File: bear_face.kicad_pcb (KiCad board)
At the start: 2 copper layers, 301.7 x 112.6 mm, 192 parts, among them J1 USB_B_Micro, SW1 SW_Push, U1 ATmega32U4-AU, Y1 16MHz

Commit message: Initial SMD commit
Diodes changed to SMD, short tracks added to pad2 and between adjacent diodes
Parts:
- removed G***: COLE, bear_face_silks:cbf_small_flipped
- removed G***: PASTA, bear_face_silks:pasta_small
- D1, D10, D11, D12, D13, D14, D15, D16, D17, D18, D19, D2, D20, D21, D22, D23, D24, D25, D26, D27, D28, D29, D3, D30, D31, D32, D33, D34, D35, D36, D37, D38, D39, D4, D40, D41, D42, D43, D44, D45, D46, D47, D48, D49, D5, D50, D51, D52, D53, D54, D55, D56, D57, D58, D59, D6, D60, D61, D62, D63, D64, D65, D66, D67, D68, D69, D7, D70, D71, D72, D73, D74, D75, D76, D77, D78, D79, D8, D80, D81, D82, D83, D9: footprint Keebio-Parts:Diode -> bear_face_parts:D_SOD-123; moved to B.Cu
- MX1, MX15, MX31, MX44: footprint MX_Only:MXOnly-1.5U-NoLED -> bear_face_parts:MXOnly-1.5U-NoLED
- MX10, MX11, MX12, MX13, MX14, MX16, MX17, MX18, MX19, MX2, MX20, MX21, MX22, MX23, MX24, MX25, MX26, MX27, MX28, MX3, MX30, MX32, MX33, MX34, MX35, MX36, MX37, MX38, MX39, MX4, MX40, MX41, MX42, MX43, MX45, MX47, MX48, MX49, MX5, MX50, MX51, MX52, MX53, MX54, MX55, MX56, MX57, MX59, MX6, MX61, MX62, MX63, MX64, MX65, MX66, MX67, MX68, MX69, MX7, MX70, MX72, MX73, MX78, MX79, MX8, MX80, MX81, MX82, MX83, MX9: footprint MX_Only:MXOnly-1U-NoLED -> bear_face_parts:MXOnly-1U-NoLED
- MX29: footprint MX_Only:MXOnly-2U-NoLED -> bear_face_parts:MXOnly-2U-NoLED
- MX46, MX71: footprint MX_Only:MXOnly-1.75U-NoLED -> bear_face_parts:MXOnly-1.75U-NoLED
- MX58, MX60: footprint MX_Only:MXOnly-2.25U-NoLED -> bear_face_parts:MXOnly-2.25U-NoLED
- MX74, MX75, MX76: footprint MX_Only:MXOnly-1.25U-NoLED -> bear_face_parts:MXOnly-1.25U-NoLED
- MX77: footprint MX_Only:MXOnly-6.25U-ReversedStabilizers-NoLED -> bear_face_parts:MXOnly-6.25U-ReversedStabilizers-NoLED
- SW1: footprint random-keyboard-parts:PushButton_6x6mm_TH_Pretty -> bear_face_parts:PushButton_6x6mm_TH_Pretty
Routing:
- net ROW0: track 372.4 -> 17.8 mm
- net ROW1: track 355.8 -> 15.2 mm, vias 2 -> 0
- net ROW5: track 339.8 -> 10.2 mm
- net ROW2: track 338.0 -> 17.8 mm
- net COL14: track 310.0 -> 0.00 mm
- net ROW3: track 306.9 -> 15.2 mm
- net COL13: track 289.6 -> 0.00 mm
- net GND: track 276.4 -> 0.00 mm, vias 1 -> 0
- net +5V: track 270.1 -> 0.00 mm, vias 7 -> 0
- net COL12: track 269.7 -> 0.00 mm
- net COL11: track 257.2 -> 0.00 mm
- net ROW4: track 261.6 -> 17.8 mm
- net COL10: track 229.7 -> 0.00 mm
- net COL9: track 221.0 -> 0.00 mm
- net COL1: track 219.9 -> 0.00 mm
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
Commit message: Rows, MCU caps and resistors tracked
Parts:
- moved C3 0.79 mm to (156.0, 159.0)
- moved C5 0.79 mm to (163.8, 162.1)
- moved R1 0.79 mm to (163.8, 159.0)
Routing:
- net ROW2: track 17.8 -> 296.9 mm
- net ROW3: track 15.2 -> 293.2 mm
- net ROW0: track 17.8 -> 287.0 mm
- net ROW1: track 15.2 -> 283.2 mm
- net ROW4: track 17.8 -> 258.0 mm
- net ROW5: track 10.2 -> 202.5 mm
- net GND: track 0.00 -> 92.9 mm
- net +5V: track 0.00 -> 26.5 mm, vias 0 -> 1
- net Net-(J1-Pad6): track 0.00 -> 15.7 mm
- net Net-(C2-Pad1): track 0.00 -> 11.9 mm
- net Net-(C1-Pad1): track 0.00 -> 8.91 mm
- net Net-(R1-Pad2): track 0.00 -> 8.61 mm
- net VCC: track 0.00 -> 5.95 mm
- net D+: track 0.00 -> 5.02 mm
- net D-: track 0.00 -> 5.02 mm
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
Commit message: Columns drawn
Columns drawn on F.Cu
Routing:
- net COL1: track 0.00 -> 118.8 mm
- net COL2: track 0.00 -> 115.9 mm
- net COL9: track 0.00 -> 113.0 mm
- net COL10: track 0.00 -> 112.9 mm
- net COL5: track 0.00 -> 111.0 mm
- net COL11: track 0.00 -> 108.1 mm
- net COL12: track 0.00 -> 108.1 mm
- net COL0: track 0.00 -> 108.0 mm
- net COL13: track 0.00 -> 107.9 mm
- net COL14: track 0.00 -> 101.0 mm
- net COL4: track 0.00 -> 91.0 mm
- net COL8: track 0.00 -> 90.9 mm
- net COL7: track 0.00 -> 90.9 mm
- net COL6: track 0.00 -> 90.9 mm
- net COL3: track 0.00 -> 90.9 mm

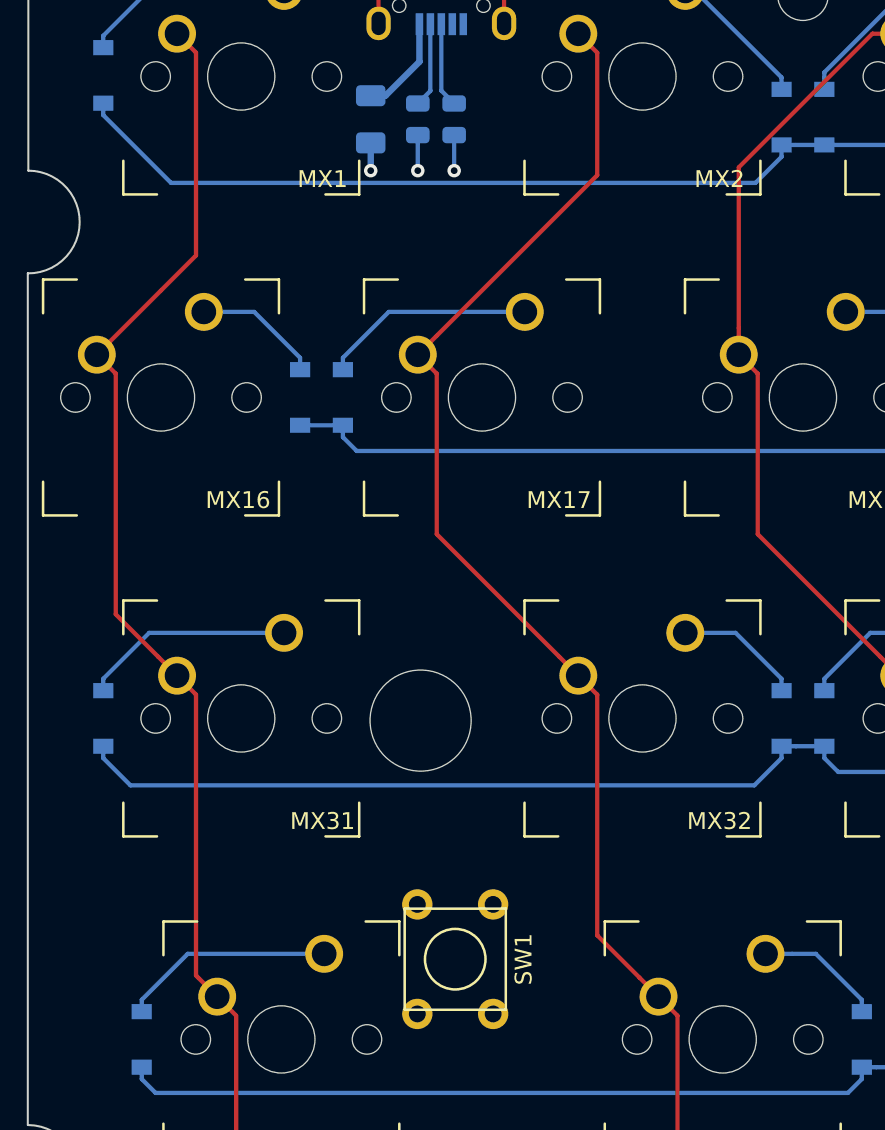
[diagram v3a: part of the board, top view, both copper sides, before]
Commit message: Changed RESET switch to SMD
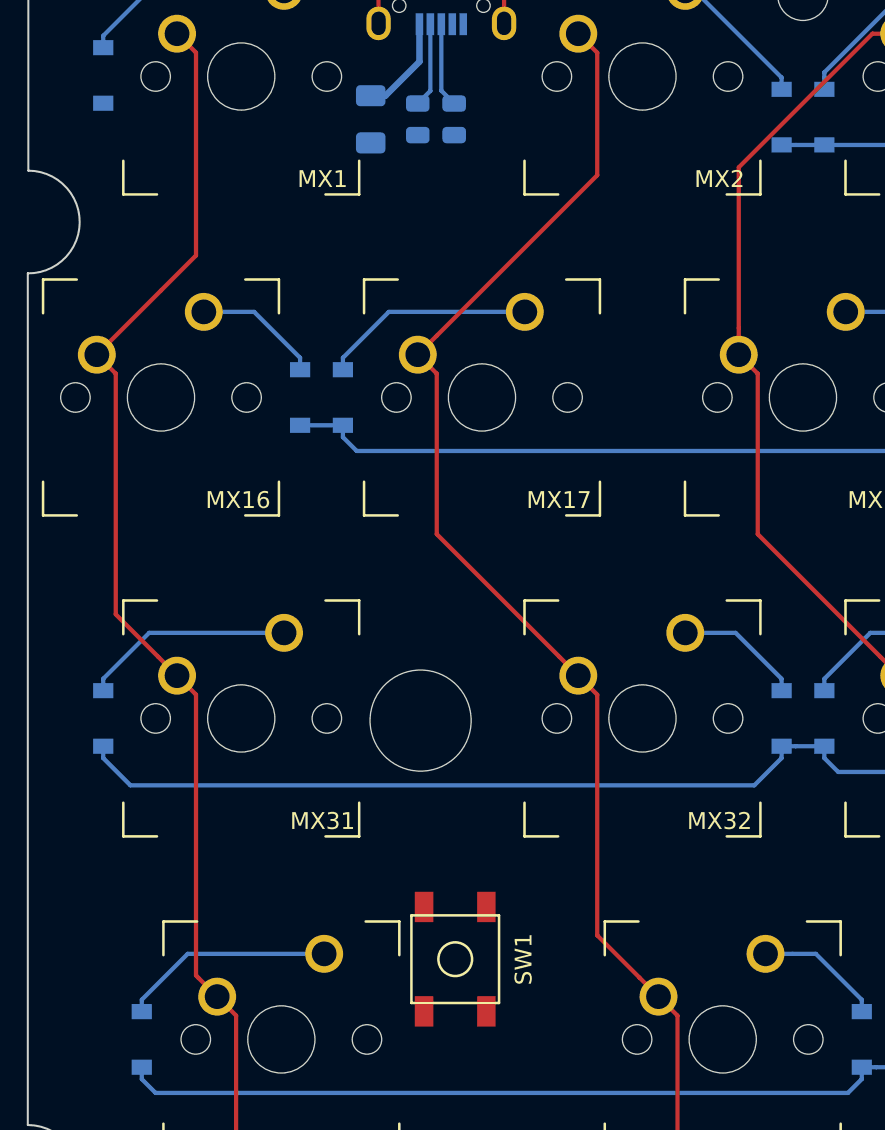
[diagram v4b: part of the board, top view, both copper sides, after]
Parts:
- SW1: footprint bear_face_parts:PushButton_6x6mm_TH_Pretty -> random-keyboard-parts:SKQG-1155865
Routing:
- net ROW0: track 287.0 -> 243.0 mm
- net Net-(R3-Pad1): track 2.11 -> 0.00 mm, vias 1 -> 0
- net Net-(R2-Pad1): track 2.11 -> 0.00 mm, vias 1 -> 0
- net +5V: track 26.5 -> 24.9 mm, vias 1 -> 0
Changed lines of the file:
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@@
     (thickness 1.6)
     (drawings 14)
-    (tracks 912)
+    (tracks 900)
     (zones 0)
     (modules 190)
@@
     (add_net "Net-(D9-Pad2)")
   )
-  (module bear_face_parts:PushButton_6x6mm_TH_Pretty (layer F.Cu)
+  (module random-keyboard-parts:SKQG-1155865 (layer F.Cu)
     (at 84.8995 130.2385 90)
+    (attr smd)
     (fp_text reference SW1 (at 0 4.064 90) (layer F.SilkS)
       (effects (font (size 1 1) (thickness 0.15)))
@@
       (effects (font (size 1 1) (thickness 0.15)))
     )
-    (fp_line (start -3 -3) (end 3 -3) (layer F.SilkS) (width 0.15))
-    (fp_line (start 3 -3) (end 3 3) (layer F.SilkS) (width 0.15))
-    (fp_line (start 3 3) (end -3 3) (layer F.SilkS) (width 0.15))
-    (fp_line (start -3 3) (end -3 -3) (layer F.SilkS) (width 0.15))
-    (fp_circle (center 0 0) (end 1.27 -1.27) (layer F.SilkS) (width 0.15))
-    (pad 4 thru_hole circle (at -3.25 -2.25 90) (size 1.8 1.8) (drill 1) (layers *.Cu *.Mask))
-    (pad 3 thru_hole circle (at 3.25 2.25 90) (size 1.8 1.8) (drill 1) (layers *.Cu *.Mask))
-    (pad 2 thru_hole circle (at -3.25 2.25 90) (size 1.8 1.8) (drill 1) (layers *.Cu *.Mask)
+    (fp_line (start -2.6 -2.6) (end 2.6 -2.6) (layer F.SilkS) (width 0.15))
+    (fp_line (start 2.6 -2.6) (end 2.6 2.6) (layer F.SilkS) (width 0.15))
+    (fp_line (start 2.6 2.6) (end -2.6 2.6) (layer F.SilkS) (width 0.15))
+    (fp_line (start -2.6 2.6) (end -2.6 -2.6) (layer F.SilkS) (width 0.15))
+    (fp_circle (center 0 0) (end 1 0) (layer F.SilkS) (width 0.15))
+    (fp_line (start -4.2 -2.6) (end 4.2 -2.6) (layer F.Fab) (width 0.15))
+    (fp_line (start 4.2 -2.6) (end 4.2 -1.2) (layer F.Fab) (width 0.15))
+    (fp_line (start 4.2 -1.1) (end 2.6 -1.1) (layer F.Fab) (width 0.15))
+    (fp_line (start 2.6 -1.1) (end 2.6 1.1) (layer F.Fab) (width 0.15))
+    (fp_line (start 2.6 1.1) (end 4.2 1.1) (layer F.Fab) (width 0.15))
+    (fp_line (start 4.2 1.1) (end 4.2 2.6) (layer F.Fab) (width 0.15))
+    (fp_line (start 4.2 2.6) (end -4.2 2.6) (layer F.Fab) (width 0.15))
+    (fp_line (start -4.2 2.6) (end -4.2 1.1) (layer F.Fab) (width 0.15))
+    (fp_line (start -4.2 1.1) (end -2.6 1.1) (layer F.Fab) (width 0.15))
+    (fp_line (start -2.6 1.1) (end -2.6 -1.1) (layer F.Fab) (width 0.15))
+    (fp_line (start -2.6 -1.1) (end -4.2 -1.1) (layer F.Fab) (width 0.15))
+    (fp_line (start -4.2 -1.1) (end -4.2 -2.6) (layer F.Fab) (width 0.15))
+    (fp_circle (center 0 0) (end 1 0) (layer F.Fab) (width 0.15))
+    (fp_line (start -2.6 -1.1) (end -1.1 -2.6) (layer F.Fab) (width 0.15))
+    (fp_line (start 2.6 -1.1) (end 1.1 -2.6) (layer F.Fab) (width 0.15))
+    (fp_line (start 2.6 1.1) (end 1.1 2.6) (layer F.Fab) (width 0.15))
+    (fp_line (start -2.6 1.1) (end -1.1 2.6) (layer F.Fab) (width 0.15))
+    (pad 4 smd rect (at -3.1 1.85 90) (size 1.8 1.1) (layers F.Cu F.Paste F.Mask))
+    (pad 3 smd rect (at 3.1 -1.85 90) (size 1.8 1.1) (layers F.Cu F.Paste F.Mask))
+    (pad 2 smd rect (at -3.1 -1.85 90) (size 1.8 1.1) (layers F.Cu F.Paste F.Mask)
       (net 113 "Net-(R1-Pad2)"))
-    (pad 1 thru_hole circle (at 3.25 -2.25 90) (size 1.8 1.8) (drill 1) (layers *.Cu *.Mask)
+    (pad 1 smd rect (at 3.1 1.85 90) (size 1.8 1.1) (layers F.Cu F.Paste F.Mask)
       (net 84 GND))
   )
@@
   (segment (start 104.267 81.914) (end 105.121 81.914) (width 0.254) (layer B.Cu) (net 85))
   (segment (start 105.121 81.914) (end 106.807 81.914) (width 0.254) (layer B.Cu) (net 85))
-  (segment (start 104.267 82.618) (end 104.267 81.914) (width 0.254) (layer B.Cu) (net 85))
-  (segment (start 68.032501 84.166001) (end 102.718999 84.166001) (width 0.254) (layer B.Cu) (net 85))
-  (segment (start 64.008 80.1415) (end 68.032501 84.166001) (width 0.254) (layer B.Cu) (net 85))
-  (segment (start 102.718999 84.166001) (end 104.267 82.618) (width 0.254) (layer B.Cu) (net 85))
-  (segment (start 64.008 79.4375) (end 64.008 80.1415) (width 0.254) (layer B.Cu) (net 85))
   (segment (start 142.367 80.205) (end 142.367 79.501) (width 0.254) (layer B.Cu) (net 85))
   (segment (start 140.658 81.914) (end 142.367 80.205) (width 0.254) (layer B.Cu) (net 85))
@@
   (segment (start 155.864 160.06525) (end 155.864 163.21) (width 0.254) (layer B.Cu) (net 111))
   (segment (start 156.8935 159.03575) (end 155.864 160.06525) (width 0.254) (layer B.Cu) (net 111))
-  (via (at 79.883 83.439) (size 0.8) (drill 0.4) (layers F.Cu B.Cu) (net 112))
-  (segment (start 79.883 81.791) (end 79.883 83.439) (width 0.381) (layer B.Cu) (net 112))
   (segment (start 149.964 173.741) (end 149.964 173.11) (width 0.381) (layer B.Cu) (net 112))
   (segment (start 147.7615 175.9435) (end 149.964 173.741) (width 0.381) (layer B.Cu) (net 112))
@@
   (segment (start 162.07799 162.776418) (end 162.8925 163.590928) (width 0.254) (layer B.Cu) (net 113))
   (segment (start 162.8925 165.730862) (end 162.666112 165.95725) (width 0.254) (layer B.Cu) (net 113))
-  (via (at 84.836 83.439) (size 0.8) (drill 0.4) (layers F.Cu B.Cu) (net 114))
-  (segment (start 84.836 81.3285) (end 84.836 83.439) (width 0.254) (layer B.Cu) (net 114))
-  (segment (start 82.677 81.3285) (end 82.677 81.816) (width 0.254) (layer B.Cu) (net 115))
-  (segment (start 82.677 81.816) (end 82.677 83.439) (width 0.254) (layer B.Cu) (net 115))
-  (via (at 82.677 83.439) (size 0.8) (drill 0.4) (layers F.Cu B.Cu) (net 115))
   (segment (start 151.9405 175.0865) (end 151.864 175.01) (width 0.254) (layer B.Cu) (net 116))
   (segment (start 151.9405 177.8) (end 151.9405 175.0865) (width 0.254) (layer B.Cu) (net 116))

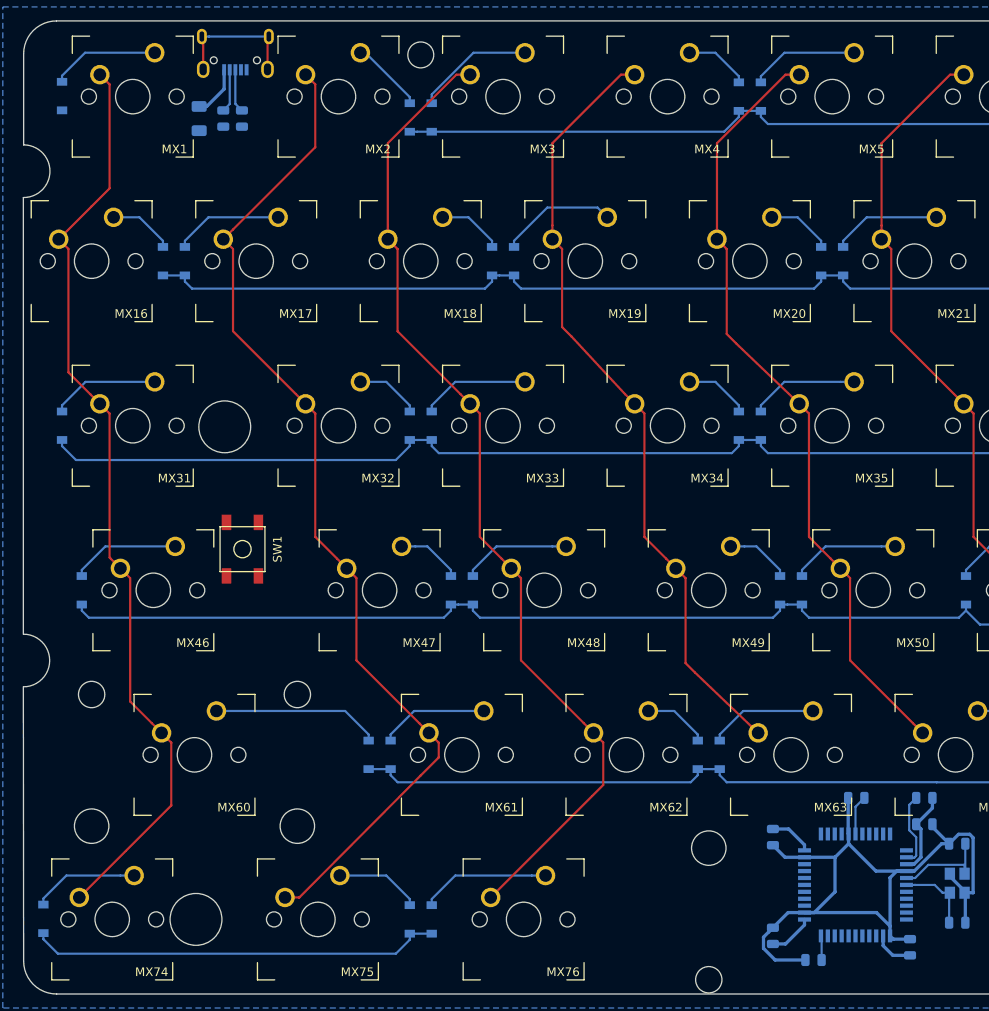
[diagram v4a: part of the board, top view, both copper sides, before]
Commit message: dPairs, left side MCU tracked
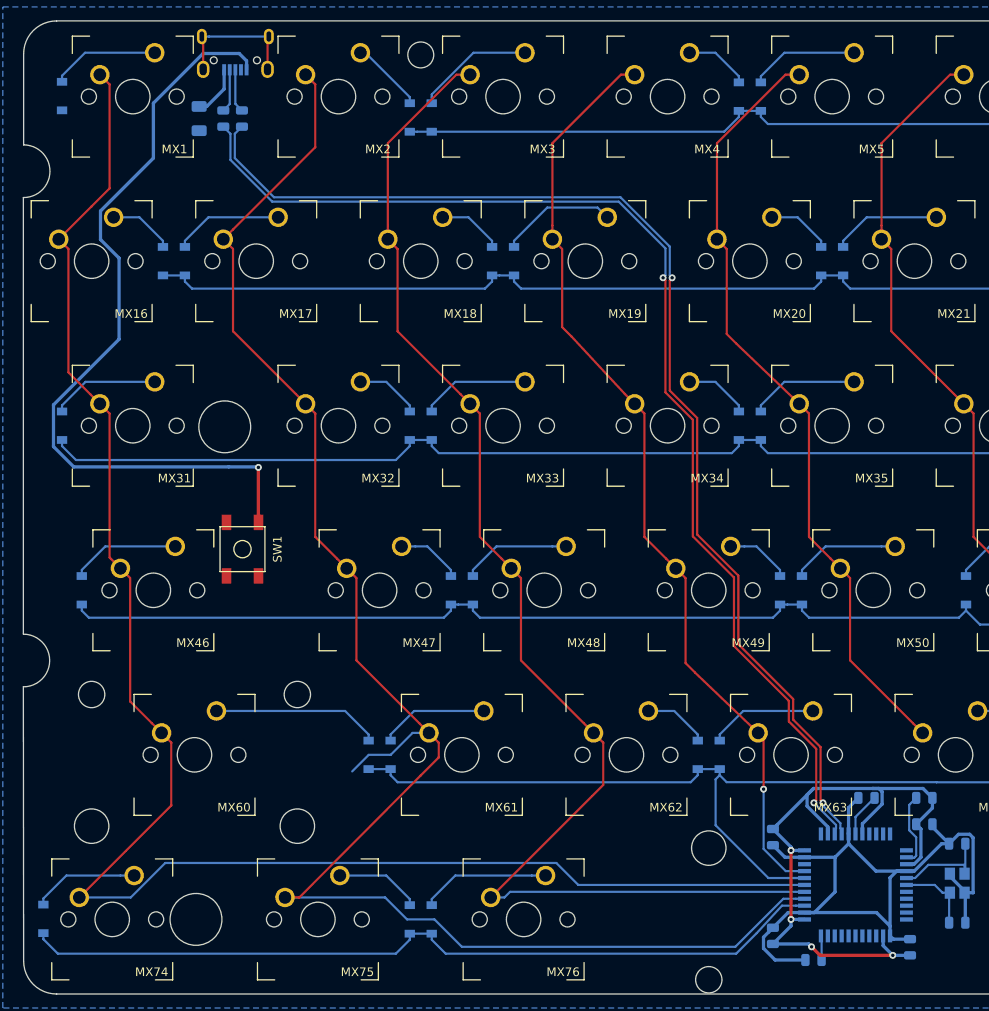
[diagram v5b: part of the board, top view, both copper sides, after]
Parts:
- moved C3 1.17 mm to (157.1, 159.0)
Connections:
- net Net-(R2-Pad1) renamed RD+
- net Net-(R3-Pad1) renamed RD-
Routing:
- net RD-: track 0.00 -> 135.3 mm, vias 0 -> 2
- net RD+: track 0.00 -> 135.0 mm, vias 0 -> 2
- net GND: track 92.9 -> 185.4 mm, vias 0 -> 1
- net COL0: track 108.0 -> 194.6 mm
- net COL1: track 118.8 -> 194.3 mm
- net +5V: track 24.9 -> 81.7 mm, vias 0 -> 4
- net ROW5: track 202.5 -> 249.4 mm
- net COL2: track 115.9 -> 152.5 mm
- net ROW4: track 258.0 -> 278.8 mm
- net COL3: track 90.9 -> 110.4 mm, vias 0 -> 1

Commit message: Tracks finished, DRC check passed, tracks and vias cleaned up
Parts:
- moved C6 0.51 mm to (146.8, 175.0)
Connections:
- U1 pad 8: ROW2 -> ROW0
- U1 pad 9: ROW0 -> ROW2
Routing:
- net COL14: track 101.0 -> 313.8 mm
- net COL13: track 107.9 -> 292.0 mm, vias 0 -> 1
- net COL12: track 108.1 -> 271.4 mm, vias 0 -> 1
- net COL11: track 108.1 -> 248.8 mm, vias 0 -> 1
- net ROW0: track 243.0 -> 378.6 mm, vias 0 -> 4
- net COL10: track 112.9 -> 243.4 mm, vias 0 -> 1
- net +5V: track 81.7 -> 205.9 mm, vias 4 -> 5
- net COL9: track 113.0 -> 225.2 mm, vias 0 -> 1
- net Net-(R1-Pad2): track 8.61 -> 116.8 mm, vias 0 -> 3
- net COL8: track 90.9 -> 186.2 mm, vias 0 -> 1
- net ROW1: track 283.2 -> 363.6 mm, vias 0 -> 2
- net COL7: track 90.9 -> 168.8 mm, vias 0 -> 1
- net GND: track 185.4 -> 262.3 mm, vias 1 -> 4
- net COL6: track 90.9 -> 149.5 mm, vias 0 -> 1
- net ROW5: track 249.4 -> 306.8 mm
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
